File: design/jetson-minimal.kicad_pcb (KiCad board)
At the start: 4 copper layers, 80 x 79.2 mm, 86 parts, among them J2 RJ45_RB1-125B8G1A, J3 Jack-DC, J4 power in, J5 2309414-1, J6 Conn_01x04_Male, J7 USB_C_Receptacle, J8 PROG, J9 reset, Q1 DMN26D0UT-7, Q2 DMN26D0UT-7, Q3 DMN26D0UT-7, Q4 DMN26D0UT-7, Q5 DMN26D0UT-7, Q6 DMN26D0UT-7, U1 74LVC1G126, U2 TLV62569DDC, U3 TLV70018DCKT, U4 74LVC1G126

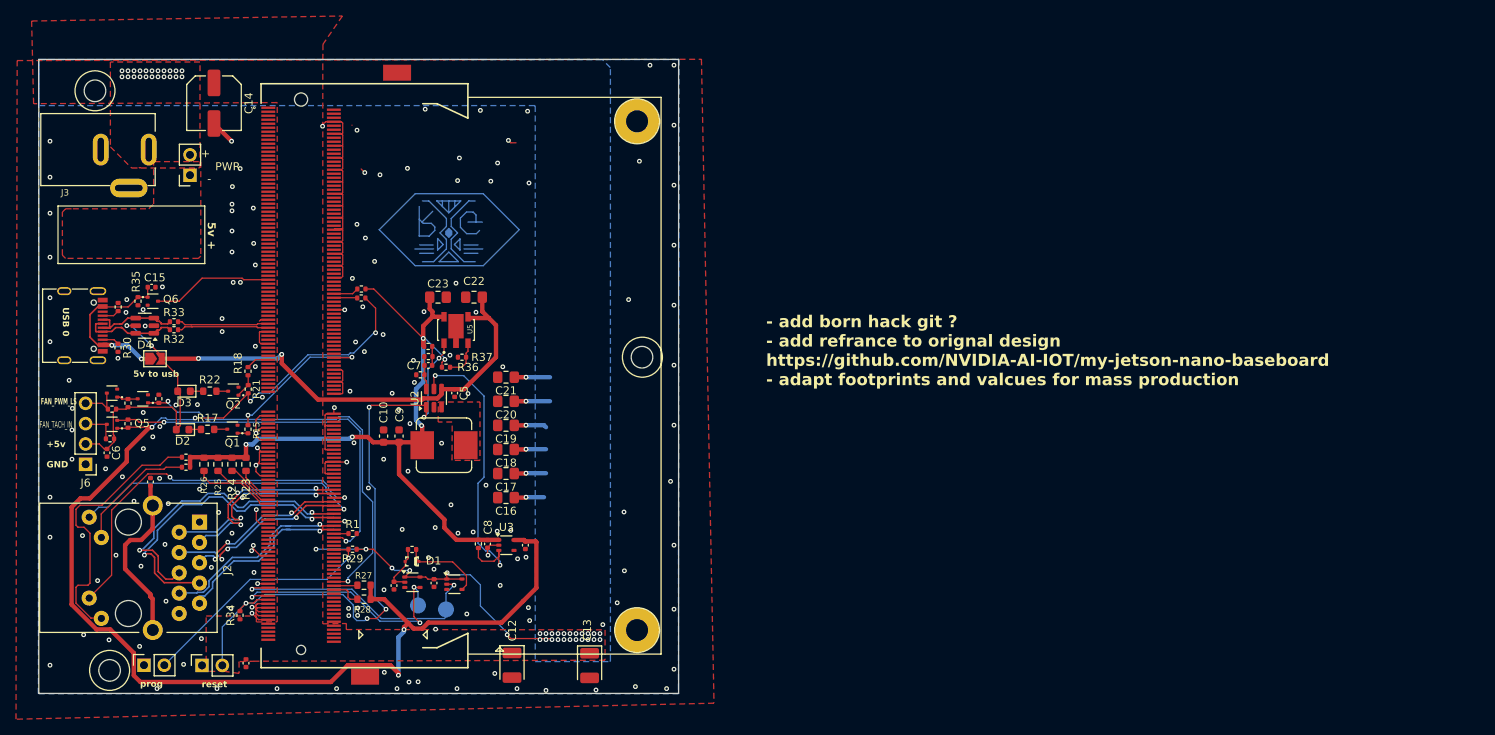
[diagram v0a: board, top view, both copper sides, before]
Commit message: updaed some compoent footprints and layouts to make it easier for manufacturing
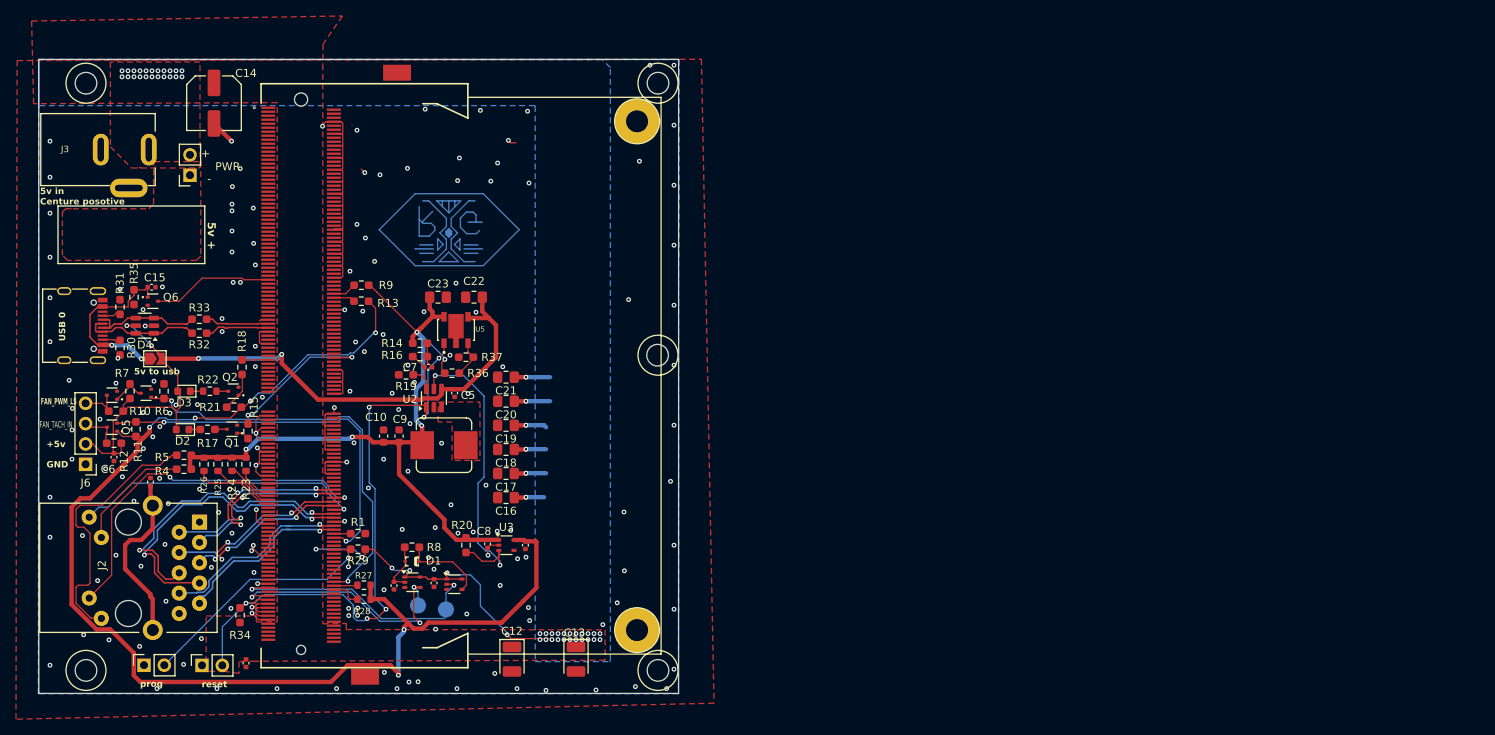
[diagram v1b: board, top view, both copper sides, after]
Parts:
- R1, R10, R11, R12, R13, R14, R15, R16, R18, R19, R20, R21, R29, R30, R31, R32, R33, R34, R36, R37, R4, R5, R6, R7, R8, R9: footprint Resistor_SMD:R_0402_1005Metric -> Resistor_SMD:R_0603_1608Metric_Pad0.98x0.95mm_HandSolder
- R17: footprint Resistor_SMD:R_0603_1608Metric -> Resistor_SMD:R_0603_1608Metric_Pad0.98x0.95mm_HandSolder
- R35: value 1M -> 100k; footprint Resistor_SMD:R_0402_1005Metric -> Resistor_SMD:R_0603_1608Metric_Pad0.98x0.95mm_HandSolder
- moved R32 3.19 mm to (3.66, 38.5)
- moved R33 3.18 mm to (3.66, 36.8)
- moved R21 2.87 mm to (8.00, 47.8), turned to 180 degrees
- moved C13 1.88 mm to (50.8, 79.2)
- moved R19 1.79 mm to (29.5, 43.7)
- moved R20 1.56 mm to (37.0, 65.0)
- moved R7 1.51 mm to (-5.00, 45.8)
- moved R11 1.22 mm to (-4.25, 50.5)
- moved R6 1.15 mm to (-0.75, 45.8)
- moved R14 1.10 mm to (31.2, 39.8)
- moved R36 1.06 mm to (35.2, 43.5)
- moved R16 1.05 mm to (31.2, 41.4)
- moved C6 1.03 mm to (-7.00, 54.0)
- moved R18 0.90 mm to (9.00, 42.8)
- moved Q3 0.80 mm to (-3.00, 46.0)
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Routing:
- net USB0_D_N: track 11.5 -> 7.96 mm
- net USB0_D_P: track 11.5 -> 8.10 mm
- net /USB0_FILT_N: track 12.0 -> 14.9 mm
- net /USB0_FILT_P: track 12.1 -> 15.0 mm
- net +5V: track 160.5 -> 162.8 mm
- net /3V3BUCK_FB: track 4.16 -> 6.48 mm
- net Net-(Q2-G): track 3.00 -> 4.91 mm
- net +3.3V: track 90.7 -> 92.6 mm
- net /FAN_PWM_INV: track 2.69 -> 4.51 mm
- net /VBUS_USB0: track 20.8 -> 22.1 mm
- net /3V3BUCK_CAP_IN: track 2.38 -> 3.27 mm
- net +1V8: track 160.2 -> 159.5 mm
- net Net-(J2-PadL3): track 15.4 -> 14.7 mm
- net 3V3_PGOOD: track 38.6 -> 39.2 mm
- net Net-(J2-PadL1): track 34.2 -> 33.7 mm
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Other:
- outline, holes or cut-outs redrawn
- board text added: "5V, 5A 'Max'"
- board text added: "5v in Centure posotive"
- board text added: "https://github.com/Richard42Graham/that-jetson-baseboard"
- board text removed: "- add born hack git ? - add refrance to orignal design https://github.com/NVIDIA-AI-IOT/my-jetson-nano-baseboard - adapt footprints and valcues for mass production"
- board text removed: "5V, 4A 'Max'"

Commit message: refinemnet
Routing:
- net ENET_LED0: track 36.5 -> 38.1 mm
- net ENET_LED1: track 45.9 -> 46.9 mm
- net GND: vias 177 -> 178
- added copper zone on In1.Cu, net GND
- added copper zone on In2.Cu, net GND
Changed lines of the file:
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@@
 	)
 	(via
+		(at 6 71.5)
+		(size 0.6)
+		(drill 0.3)
+		(layers "F.Cu" "B.Cu")
+		(net 1)
+	)
+	(via
 		(at -15 29)
 		(size 0.6)
@@
 	)
 	(segment
-		(start 20.854042 59.049242)
-		(end 19.8048 58)
+		(start 0.4 56.9)
+		(end 0 56.5)
 		(width 0.1524)
 		(layer "B.Cu")
@@
 	)
 	(segment
-		(start 19.126252 56.9452)
-		(end 18.9452 56.9452)
+		(start 15.25 56)
+		(end 14.35 56.9)
 		(width 0.1524)
 		(layer "B.Cu")
@@
 	)
 	(segment
-		(start 19.8048 58)
-		(end 19.8048 57.623748)
+		(start 19.5 56)
+		(end 15.25 56)
 		(width 0.1524)
 		(layer "B.Cu")
@@
 	)
 	(segment
-		(start 19.8048 57.623748)
-		(end 19.126252 56.9452)
+		(start 21.83165 58.33165)
+		(end 19.5 56)
 		(width 0.1524)
 		(layer "B.Cu")
@@
 	(segment
 		(start 21.83165 59.049242)
-		(end 20.854042 59.049242)
-		(width 0.1524)
-		(layer "B.Cu")
-		(net 171)
-	)
-	(segment
-		(start 18.9452 56.9452)
-		(end 18.9 56.9)
-		(width 0.1524)
-		(layer "B.Cu")
-		(net 171)
-	)
-	(segment
-		(start 0.4 56.9)
-		(end 0 56.5)
+		(end 21.83165 58.33165)
 		(width 0.1524)
 		(layer "B.Cu")
@@
 	)
 	(segment
-		(start 18.9 56.9)
+		(start 14.35 56.9)
 		(end 0.4 56.9)
 		(width 0.1524)
@@
 	)
 	(segment
-		(start 21.75 60.5)
-		(end 19.5 58.25)
+		(start 21.5 59.75)
+		(end 21.5 59.465146)
 		(width 0.1524)
 		(layer "B.Cu")
@@
 	)
 	(segment
-		(start -8.91 60.25)
-		(end -10.12 61.46)
+		(start 21.30305 58.234102)
+		(end 19.373748 56.3048)
+		(width 0.1524)
+		(layer "B.Cu")
+		(net 174)
+	)
+	(segment
+		(start 21.30305 59.268196)
+		(end 21.30305 58.234102)
+		(width 0.1524)
+		(layer "B.Cu")
+		(net 174)
+	)
+	(segment
+		(start 15.4452 56.3048)
+		(end 14.5452 57.2048)
+		(width 0.1524)
+		(layer "B.Cu")
+		(net 174)
+	)
+	(segment
+		(start 14.5452 57.2048)
+		(end -5.8648 57.2048)
 		(width 0.1524)
 		(layer "B.Cu")
@@
 	)
 	(segment
-		(start -4.75 57.25)
-		(end -7.75 60.25)
+		(start 21.75 60.5)
+		(end 21.75 60)
 		(width 0.1524)
 		(layer "B.Cu")
@@
 	)
 	(segment
-		(start 19.5 57.75)
-		(end 19 57.25)
+		(start -5.8648 57.2048)
+		(end -10.12 61.46)
 		(width 0.1524)
 		(layer "B.Cu")
@@
 	)
 	(segment
-		(start 19.5 58.25)
-		(end 19.5 57.75)
+		(start 21.75 60)
+		(end 21.5 59.75)
 		(width 0.1524)
 		(layer "B.Cu")
@@
 	)
 	(segment
-		(start -7.75 60.25)
-		(end -8.91 60.25)
+		(start 19.373748 56.3048)
+		(end 15.4452 56.3048)
 		(width 0.1524)
 		(layer "B.Cu")
@@
 	)
 	(segment
-		(start 19 57.25)
-		(end -4.75 57.25)
+		(start 21.5 59.465146)
+		(end 21.30305 59.268196)
 		(width 0.1524)
 		(layer "B.Cu")
@@
 			)
 		)
+	)
+	(zone
+		(net 1)
+		(net_name "GND")
+		(layer "In1.Cu")
+		(hatch edge 0.5)
+		(priority 5)
+		(connect_pads
+			(clearance 0.1)
+		)
+		(min_thickness 0.25)
+		(filled_areas_thickness no)
+		(fill yes
+			(thermal_gap 0.5)
+			(thermal_bridge_width 0.5)
+		)
+		(polygon
+			(pts
+				(xy 69 89) (xy -22.25 89) (xy -22.25 1.25) (xy 69 1.25) (xy 69 2.5)
+			)
+		)
+	)
+	(zone
+		(net 1)
+		(net_name "GND")
+		(layer "In2.Cu")
+		(hatch edge 0.5)
+		(priority 5)
+		(connect_pads
+			(clearance 0.1)
+		)
+		(min_thickness 0.25)
+		(filled_areas_thickness no)
+		(fill yes
+			(thermal_gap 0.5)
+			(thermal_bridge_width 0.5)
+		)
+		(polygon
+			(pts
+				(xy 73.5 90.25) (xy -17.75 90.25) (xy -17.75 2.5) (xy 73.5 2.5) (xy 73.5 3.75)
+			)
+		)
